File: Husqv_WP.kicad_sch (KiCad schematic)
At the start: 16 parts, among them U1 MIC4120YME

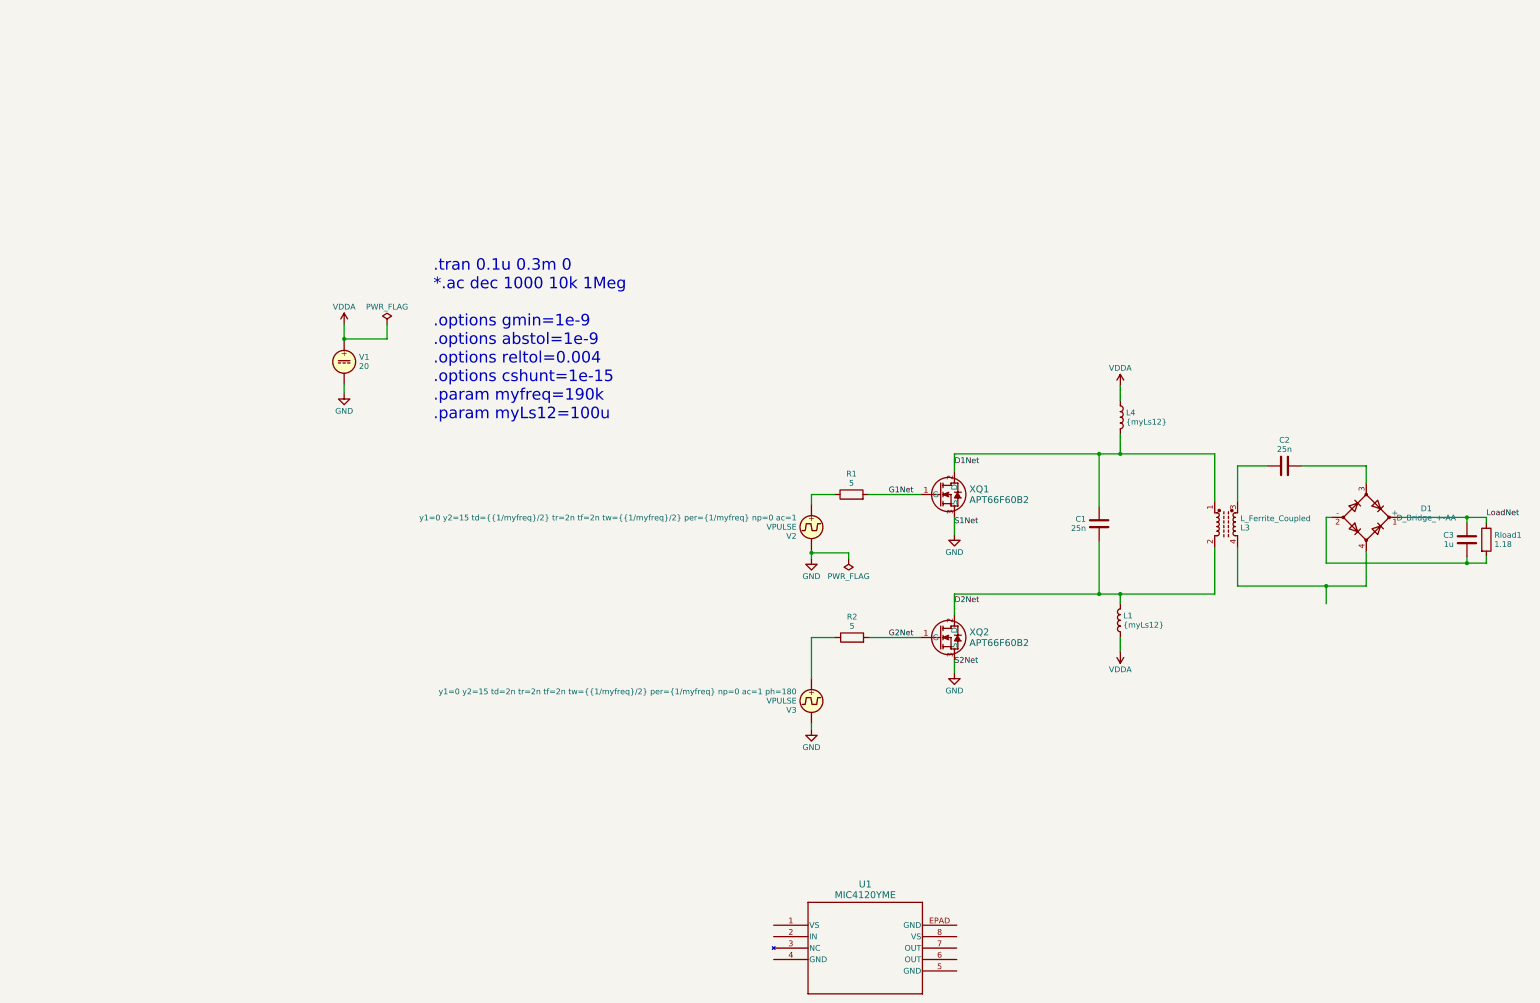
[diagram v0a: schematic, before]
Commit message: version with step-script (not plotting) before trying stepping in the ppp_SiC version instead
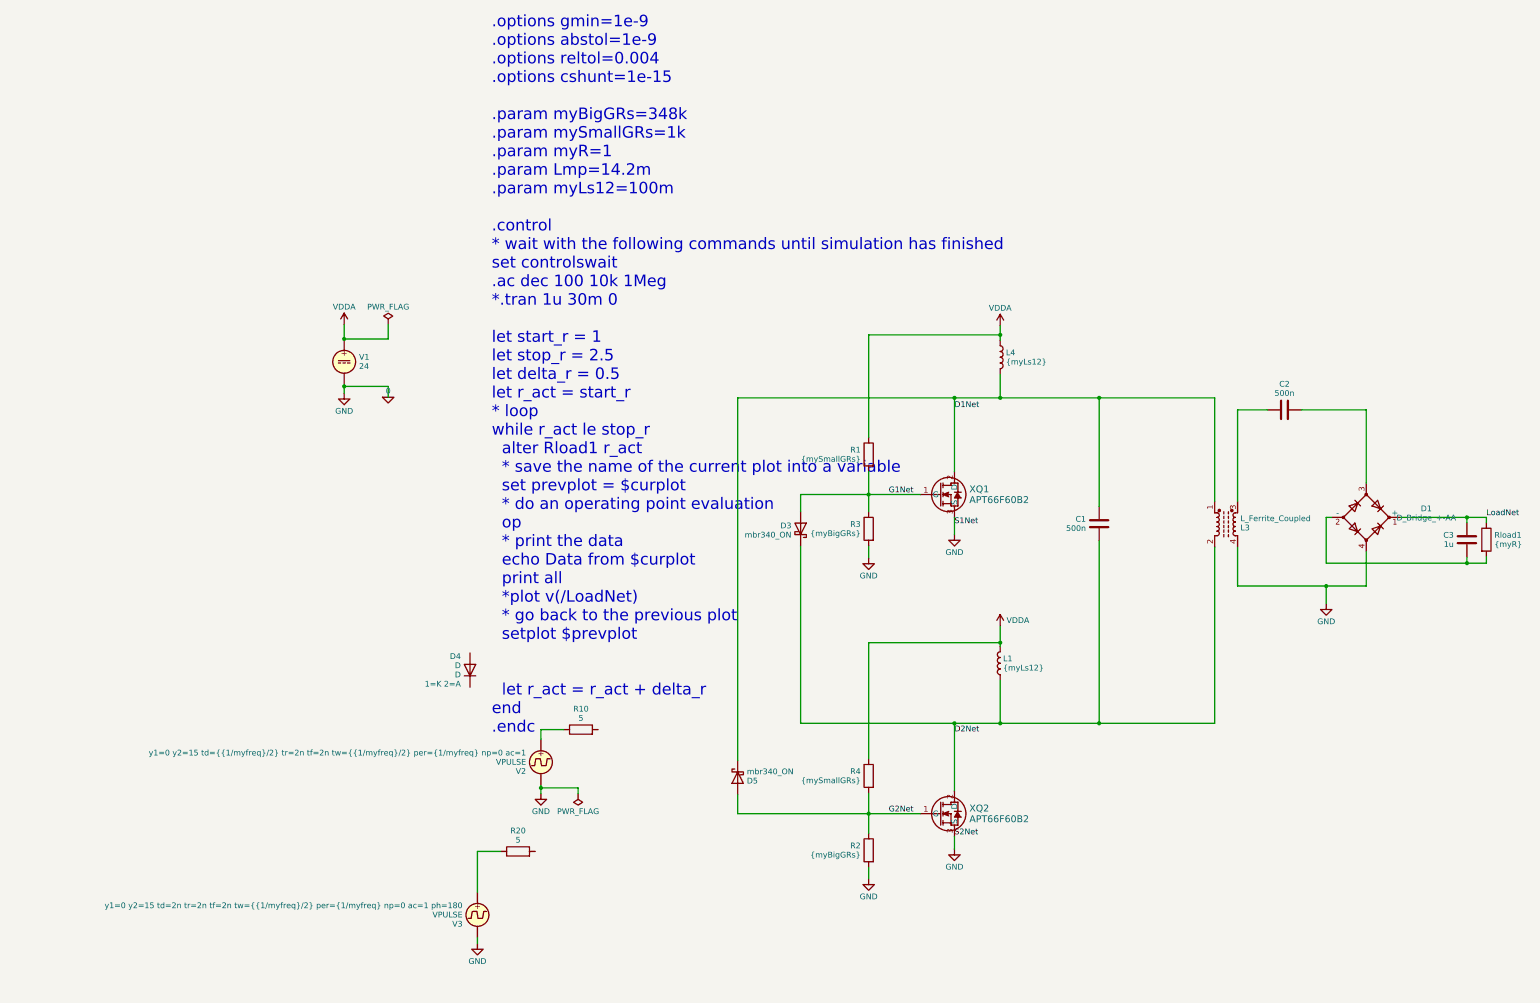
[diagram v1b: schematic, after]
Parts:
- removed U1: MIC4120YME, SOIC8_EPAD_ME_MCH, symbol myLibSymbols:MIC4120YME
- added D3, D5: mbr340_ON, Diode_THT:D_DO-201AD_P15.24mm_Horizontal, symbol Diode:MBR340
- added D4: D, symbol Simulation_SPICE:D
- added R10, R20: 5, symbol Device:R
- added R3: {myBigGRs}, symbol Device:R
- added R4: {mySmallGRs}, symbol Device:R
- C1, C2: value 25n -> 500n
- R1: value 5 -> {mySmallGRs}
- R2: value 5 -> {myBigGRs}
- Rload1: value 1.18 -> {myR}
- V1: value 20 -> 24
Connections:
- net GND is gone; now on net 0: V1.2, V2.2, V3.2, XQ1.3 (S), XQ2.3 (S)
- net D1Net: now also D5.1 (K)
- net D2Net: now also L1.1, D3.1 (K); no longer L1.2
- net G1Net: now also D3.2 (A), R3.1
- net G2Net: now also R2.1, D5.2 (A), R4.2; no longer R2.2
- net VDDA: now also L1.2, R1.1, R4.1; no longer L1.1
- net at V3.1: now also R20.1; no longer R2.1
- net 0: now reaches D1.4, L3.4
- net 0: now also R2.2, R3.2
- net at V2.1: now also R10.1; no longer R1.1
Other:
- note added: ".options gmin=1e-9 .options abstol=1e-9 .options reltol=0.004 .options cshunt=1e-15 .param myBigGRs=348k .param mySmallGRs=1k .param myR=1 .param Lmp=14.2m .param myLs12=100m .control * wait with the following commands until simulation has finished set controlswait .ac dec 100 10k 1Meg *.tran 1u 30m 0 let start_r = 1 let stop_r = 2.5 let delta_r = 0.5 let r_act = start_r * loop while r_act le sto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"
- note removed: ".tran 0.1u 0.3m 0 *.ac dec 1000 10k 1Meg .options gmin=1e-9 .options abstol=1e-9 .options reltol=0.004 .options cshunt=1e-15 .param myfreq=190k .param myLs12=100u"
- moved on the sheet: C2, L4, XQ2

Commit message: committing residues wwhatever they are
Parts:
- renumbered D3 to D1, D5 to D2, D1 to Drect1
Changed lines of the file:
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@@
   (symbol (lib_id "Diode:MBR340") (at 124.587 85.09 270) (mirror x) (unit 1)
     (in_bom yes) (on_board yes) (dnp no)
-    (property "Reference" "D3" (at 122.555 84.3835 90)
+    (property "Reference" "D1" (at 122.555 84.3835 90)
       (effects (font (size 1.27 1.27)) (justify right))
     )
@@
       (project "Husqv_WP"
         (path "/78a5d0a0-367b-45cd-a8c4-6f1e567c7d52"
-          (reference "D3") (unit 1)
+          (reference "D1") (unit 1)
         )
       )
@@
   (symbol (lib_id "Diode:MBR340") (at 110.617 140.335 90) (mirror x) (unit 1)
     (in_bom yes) (on_board yes) (dnp no)
-    (property "Reference" "D5" (at 112.649 141.0415 90)
+    (property "Reference" "D2" (at 112.649 141.0415 90)
       (effects (font (size 1.27 1.27)) (justify right))
     )
@@
       (project "Husqv_WP"
         (path "/78a5d0a0-367b-45cd-a8c4-6f1e567c7d52"
-          (reference "D5") (unit 1)
+          (reference "D2") (unit 1)
         )
       )
@@
   (symbol (lib_id "Device:D_Bridge_+-AA") (at 250.19 82.55 0) (unit 1)
     (in_bom yes) (on_board yes) (dnp no) (fields_autoplaced)
-    (property "Reference" "D1" (at 263.5179 80.5957 0)
+    (property "Reference" "Drect1" (at 263.5179 80.5957 0)
       (effects (font (size 1.27 1.27)))
     )
@@
       (project "Husqv_WP"
         (path "/78a5d0a0-367b-45cd-a8c4-6f1e567c7d52"
-          (reference "D1") (unit 1)
-        )
-      )
+          (reference "Drect1") (unit 1)
+        )
+      )
